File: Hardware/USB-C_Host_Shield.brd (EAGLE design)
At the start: 53.3 x 59.7 mm, 139 parts, among them J1 USB-C, J2 GPIN, J3 GPOUT, U1 ARDUINO_UNO_R3_SHIELDNOLABELS, U2 LM1117, U3 74HC4050, U5 MAX3421, U6 3.3V/150mA, Y1 12.0mhZ

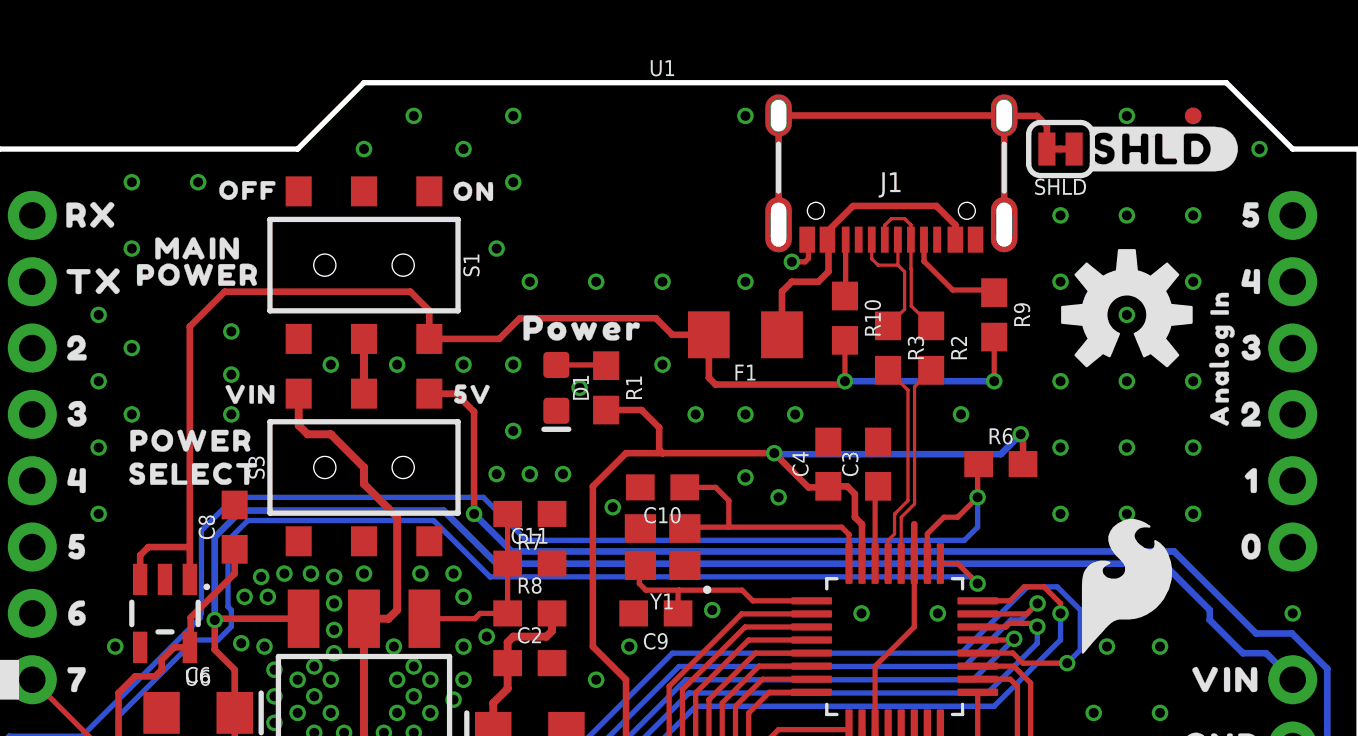
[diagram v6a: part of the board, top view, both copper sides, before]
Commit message: Added panel files and adjusted schematic notation
Ran panelization script and added those files to the repo. Adjusted the Vin input value on the schematic for people to better understand the input range.
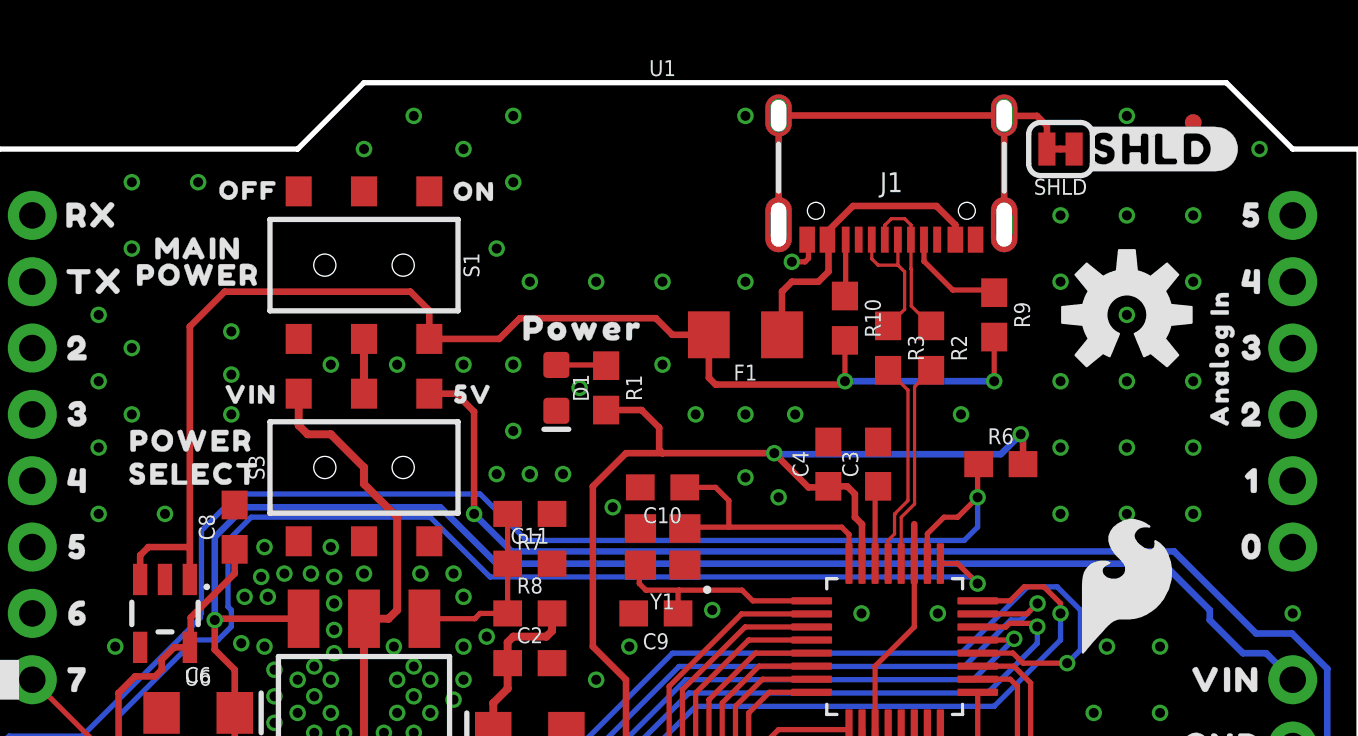
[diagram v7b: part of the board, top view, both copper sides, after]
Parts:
- moved FD3 0.25 mm to (47.0, 55.6)
- moved FD4 0.25 mm to (47.0, 55.6)
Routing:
- net GND: vias 161 -> 164
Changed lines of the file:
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@@
 <drawing>
 <settings>
-<setting alwaysvectorfont="yes"/>
+<setting alwaysvectorfont="no"/>
 <setting verticaltext="up"/>
 </settings>
@@
 <layer number="44" name="Drills" color="7" fill="1" visible="no" active="yes"/>
 <layer number="45" name="Holes" color="7" fill="1" visible="yes" active="yes"/>
-<layer number="46" name="Milling" color="3" fill="1" visible="yes" active="yes"/>
+<layer number="46" name="Milling" color="3" fill="1" visible="no" active="yes"/>
 <layer number="47" name="Measures" color="7" fill="1" visible="no" active="yes"/>
 <layer number="48" name="Document" color="7" fill="1" visible="no" active="yes"/>
@@
 <element name="FD1" library="SparkFun-Aesthetics" package="FIDUCIAL-MICRO" value="FIDUCIALUFIDUCIAL" x="2.54" y="0" smashed="yes" rot="MR0"/>
 <element name="FD2" library="SparkFun-Aesthetics" package="FIDUCIAL-MICRO" value="FIDUCIALUFIDUCIAL" x="2.54" y="0" smashed="yes" rot="R90"/>
-<element name="FD3" library="SparkFun-Aesthetics" package="FIDUCIAL-MICRO" value="FIDUCIALUFIDUCIAL" x="46.99" y="55.88" smashed="yes" rot="MR0"/>
-<element name="FD4" library="SparkFun-Aesthetics" package="FIDUCIAL-MICRO" value="FIDUCIALUFIDUCIAL" x="46.99" y="55.88" smashed="yes"/>
+<element name="FD3" library="SparkFun-Aesthetics" package="FIDUCIAL-MICRO" value="FIDUCIALUFIDUCIAL" x="46.99" y="55.626" smashed="yes" rot="MR0"/>
+<element name="FD4" library="SparkFun-Aesthetics" package="FIDUCIAL-MICRO" value="FIDUCIALUFIDUCIAL" x="46.99" y="55.626" smashed="yes"/>
 <element name="FRAME1" library="SparkFun-Aesthetics" package="CREATIVE_COMMONS" value="FRAME-LETTER" x="1.27" y="-33.02" smashed="yes">
 <attribute name="DESIGNER" value="" x="81.28" y="-111.76" size="1.778" layer="27" display="off"/>
@@
 <wire x1="47.625" y1="36.957" x2="45.847" y2="38.735" width="0.254" layer="16"/>
 <wire x1="45.847" y1="38.735" x2="20.32" y2="38.735" width="0.254" layer="16"/>
-<wire x1="20.32" y1="38.735" x2="18.288" y2="40.767" width="0.254" layer="16"/>
-<wire x1="18.288" y1="40.767" x2="10.541" y2="40.767" width="0.254" layer="16"/>
-<wire x1="10.541" y1="40.767" x2="9.525" y2="39.751" width="0.254" layer="16"/>
+<wire x1="20.32" y1="38.735" x2="18.161" y2="40.894" width="0.254" layer="16"/>
+<wire x1="18.161" y1="40.894" x2="10.668" y2="40.894" width="0.254" layer="16"/>
+<wire x1="10.668" y1="40.894" x2="9.525" y2="39.751" width="0.254" layer="16"/>
 <wire x1="9.525" y1="39.751" x2="9.525" y2="36.576" width="0.254" layer="16"/>
 <via x="9.525" y="36.576" extent="1-16" drill="0.381"/>
@@
 <via x="10.541" y="35.687" extent="1-16" drill="0.381"/>
 <via x="29.845" y="42.037" extent="1-16" drill="0.381"/>
+<via x="13.97" y="39.37" extent="1-16" drill="0.381"/>
+<via x="11.43" y="39.37" extent="1-16" drill="0.381"/>
+<via x="7.62" y="40.64" extent="1-16" drill="0.381"/>
 </signal>
 <signal name="N$7">
@@
 <wire x1="38.735" y1="37.973" x2="38.481" y2="38.227" width="0.2032" layer="16"/>
 <wire x1="38.481" y1="38.227" x2="20.066" y2="38.227" width="0.2032" layer="16"/>
-<wire x1="20.066" y1="38.227" x2="17.907" y2="40.386" width="0.2032" layer="16"/>
-<wire x1="10.795" y1="40.386" x2="10.033" y2="39.624" width="0.2032" layer="16"/>
+<wire x1="20.066" y1="38.227" x2="17.78" y2="40.513" width="0.2032" layer="16"/>
+<wire x1="10.922" y1="40.513" x2="10.033" y2="39.624" width="0.2032" layer="16"/>
 <wire x1="10.033" y1="39.624" x2="10.033" y2="37.084" width="0.2032" layer="16"/>
 <wire x1="10.033" y1="37.084" x2="10.16" y2="36.957" width="0.2032" layer="16"/>
@@
 <wire x1="8.763" y1="35.814" x2="5.842" y2="32.893" width="0.2032" layer="16"/>
 <wire x1="5.842" y1="31.242" x2="5.08" y2="30.48" width="0.2032" layer="16"/>
-<wire x1="17.907" y1="40.386" x2="10.795" y2="40.386" width="0.2032" layer="16"/>
+<wire x1="17.78" y1="40.513" x2="10.922" y2="40.513" width="0.2032" layer="16"/>
 <wire x1="5.842" y1="32.893" x2="5.842" y2="31.242" width="0.2032" layer="16"/>
 </signal>
@@
 <wire x1="8.9789" y1="36.80220625" x2="8.9789" y2="36.6649" width="0.2032" layer="16"/>
 <wire x1="38.227" y1="39.624" x2="21.463" y2="39.624" width="0.2032" layer="16"/>
-<wire x1="21.463" y1="39.624" x2="19.812" y2="41.275" width="0.2032" layer="16"/>
-<wire x1="19.812" y1="41.275" x2="10.287" y2="41.275" width="0.2032" layer="16"/>
-<wire x1="10.287" y1="41.275" x2="9.017" y2="40.005" width="0.2032" layer="16"/>
+<wire x1="21.463" y1="39.624" x2="19.685" y2="41.402" width="0.2032" layer="16"/>
+<wire x1="19.685" y1="41.402" x2="10.414" y2="41.402" width="0.2032" layer="16"/>
+<wire x1="10.414" y1="41.402" x2="9.017" y2="40.005" width="0.2032" layer="16"/>
 <wire x1="9.017" y1="40.005" x2="9.017" y2="36.84030625" width="0.2032" layer="16"/>
 <wire x1="8.9789" y1="36.6649" x2="4.445" y2="32.131" width="0.2032" layer="16"/>

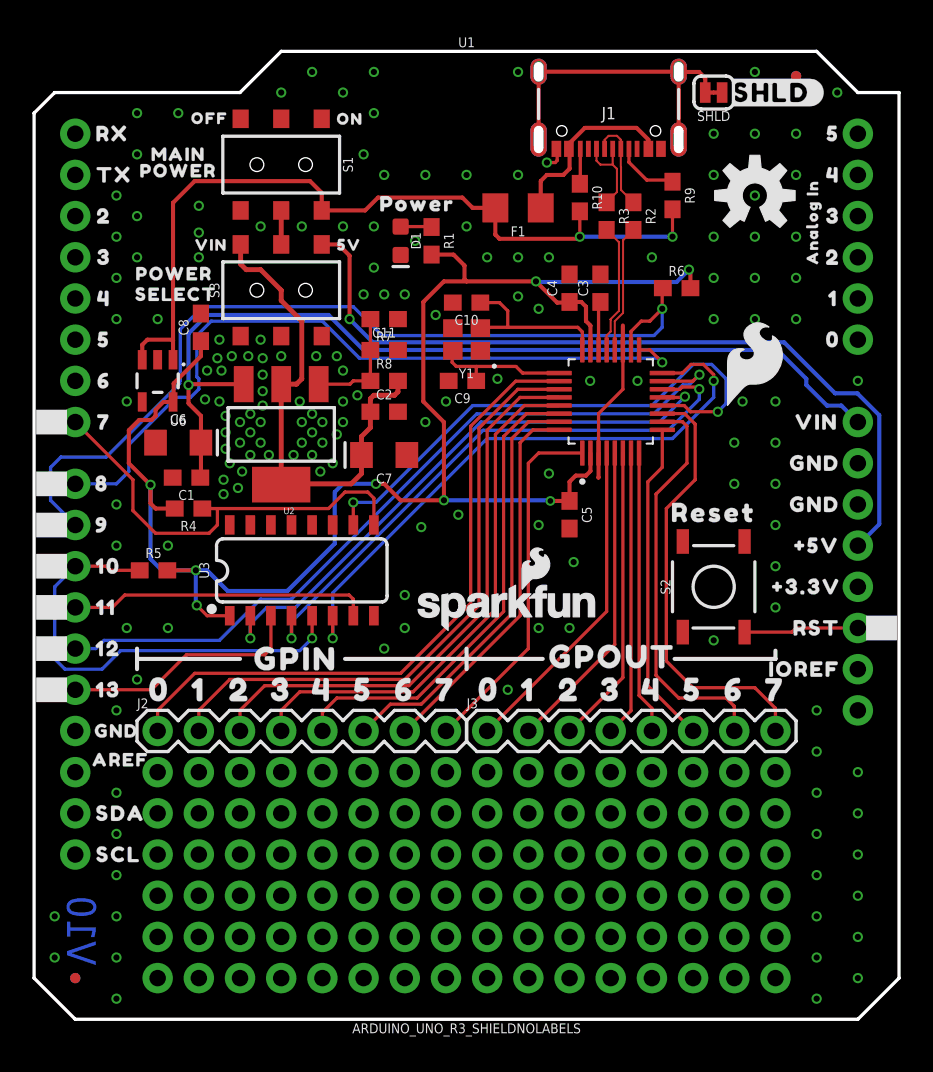
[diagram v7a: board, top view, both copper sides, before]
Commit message: Updates from design review
Moved silkscreen pin 1 indicator closer to the MAX3421 IC, added new switches into schematic to use the ancillary pads for extra protection, and added new power thermal pad on the LD1117
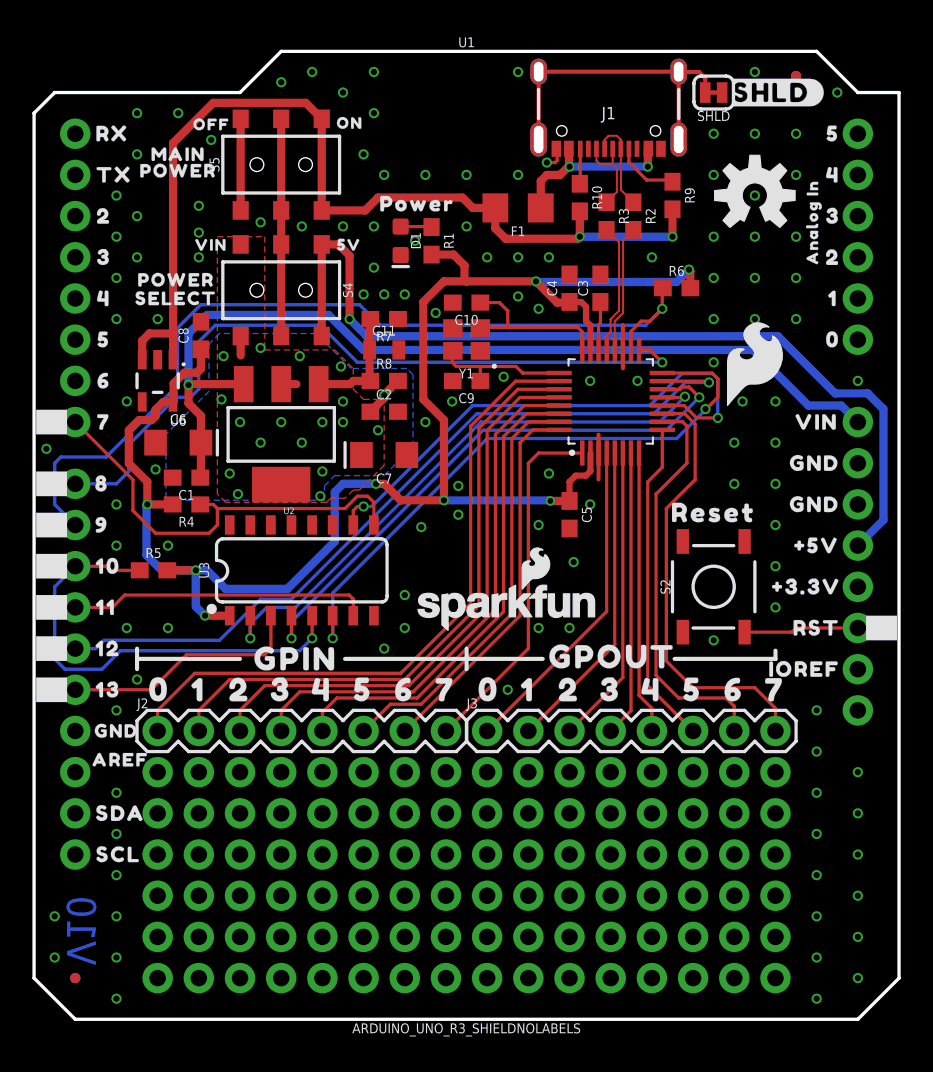
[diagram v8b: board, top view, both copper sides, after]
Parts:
- C11: device SparkFun-Capacitors:0603 -> SparkFun-Capacitors:0805
- moved C8 0.51 mm to (10.3, 39.6)
- moved U$10 0.40 mm to (8.76, 43.1)
- moved U$7 0.40 mm to (10.9, 52.6)
- moved R4 0.28 mm to (9.40, 29.2)
- moved U$13 0.25 mm to (8.76, 41.9)
- moved U$5 0.25 mm to (19.5, 52.7)
- moved C9 0.25 mm to (26.7, 36.8)
- turned S4 to 180 degrees
- turned S5 to 0 degrees
- renumbered S1 to S5, S3 to S4
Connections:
- new net N$5: S5.1, S5.4
- net 5V: now also S4.1, S4.4; no longer S4.3
- net N$2: now also S4.5, S5.5
- net N$6: now also S4.3, S4.6; no longer S4.1
- net VDD: now also S5.3, S5.6; no longer S5.1
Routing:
- net N$6: track 30.6 -> 4.75 mm, vias 0 -> 18
- net N$2: track 2.10 -> 13.4 mm
- net VDD: track 51.1 -> 59.9 mm
- net 5V: track 49.6 -> 55.9 mm
- net N$5: track 0.00 -> 5.65 mm
- net GND: track 11.4 -> 6.86 mm, vias 164 -> 122
- net 3.3V: track 102.3 -> 101.0 mm
- net INT: track 55.0 -> 53.8 mm
- net RESET-IN: track 34.1 -> 33.1 mm
- net POCI: track 47.9 -> 48.8 mm
- net VBUS: track 11.5 -> 10.8 mm, vias 0 -> 2
- net GPX: track 46.2 -> 45.6 mm
- added copper zone on layer 1, net N$6
- added copper zone on layer 16, net N$6
